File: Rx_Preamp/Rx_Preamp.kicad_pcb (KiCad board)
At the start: 2 copper layers, 97.5 x 79.5 mm, 128 parts, among them J1 Conn_Coaxial, J2 Conn_Coaxial, J3 Conn_Coaxial, J4 Conn_Coaxial, J5 Barrel_Jack_Switch, J6 Barrel_Jack_Switch, J7 ScrewTerminal01x03, SW1 SW_DIP_x04, U1 AD8429, U2 LT6350HMS8TRPBF, U3 ADA4610-1ARJZ, U4 ADA4610-1ARJZ, U5 L7805, U6 L7905, U7 ADA4610-1ARJZ, U8 PIG-LOGO, U9 PIG-LOGO

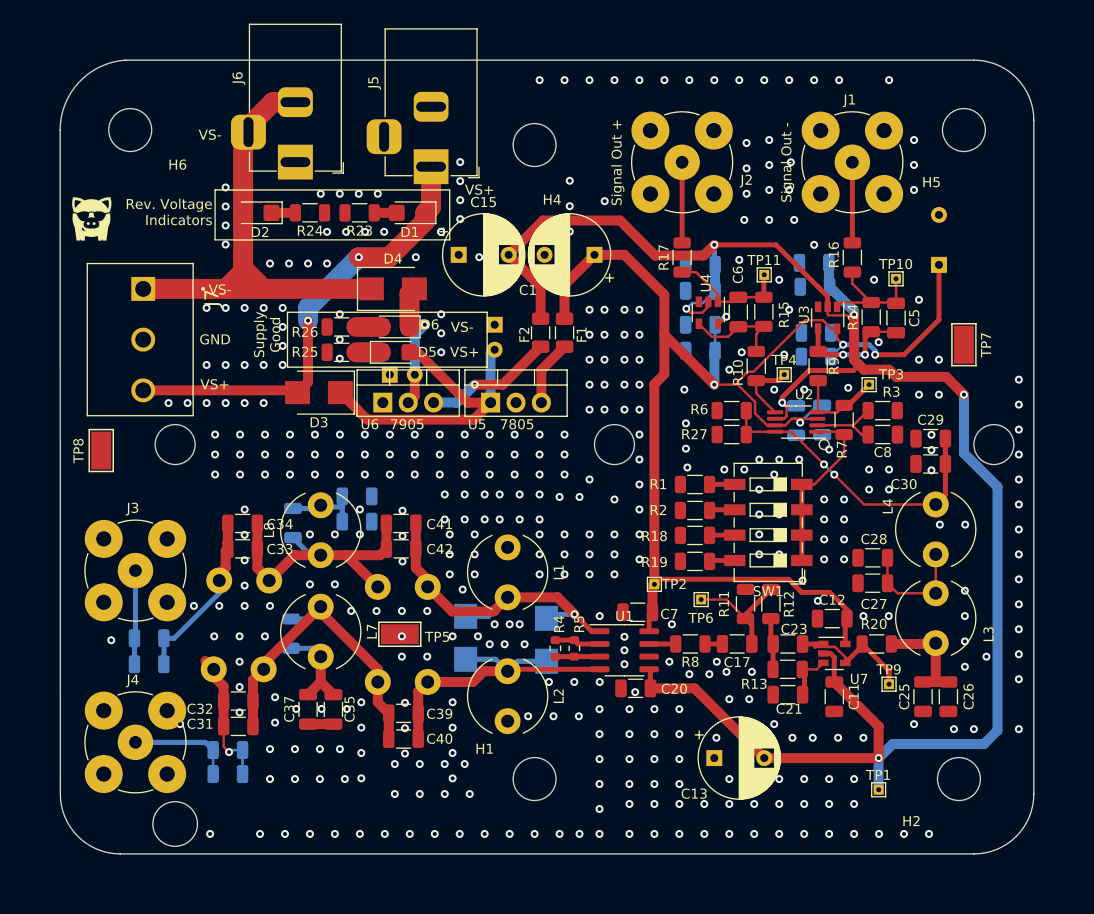
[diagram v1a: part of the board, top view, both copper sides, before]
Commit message: Modular(JFET) preamp and INA preamp
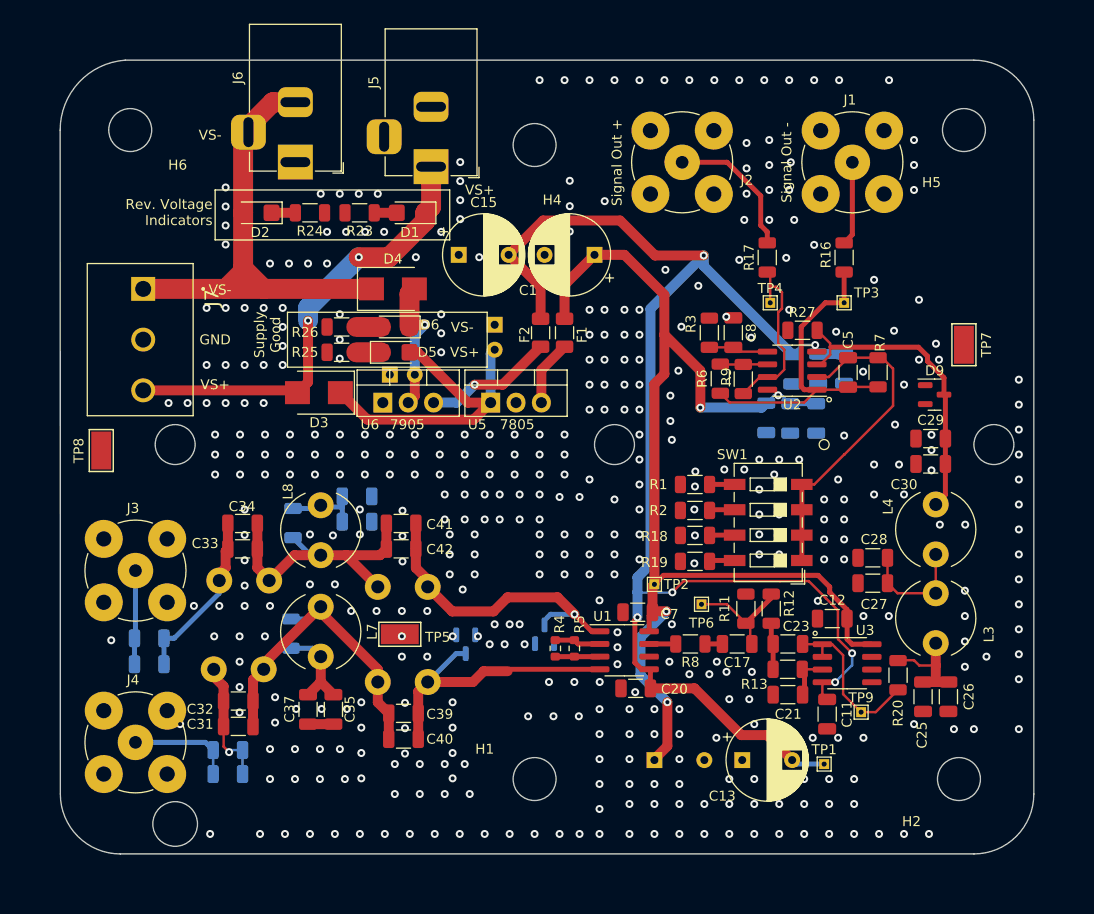
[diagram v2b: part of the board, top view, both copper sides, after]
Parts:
- removed C10, C14: 1u, Capacitor_SMD:C_1206_3216Metric
- removed C19, C4: 100n, Capacitor_SMD:C_1206_3216Metric
- removed C6: 300p, Capacitor_SMD:C_1206_3216Metric
- removed L1, L2: 1m, Inductor_THT:L_Radial_D7.8mm_P5.00mm_Fastron_07HCP
- removed R10, R14, R15: 1k, Resistor_SMD:R_1206_3216Metric
- removed TP10, TP11: TestPoint, TestPoint:TestPoint_THTPad_1.0x1.0mm_Drill0.5mm
- removed U4, U7: ADA4610-1ARJZ, Package_TO_SOT_SMD:SOT-23-5
- removed U8: PIG-LOGO, PigLogos:PIG-LOGO2
- removed U9: PIG-LOGO, Symbol:OSHW-Symbol_22.3x20mm_SilkScreen
- added D9: BAV99, Package_TO_SOT_SMD:SOT-23, F.Cu at (130.1, 116.0)
- C5: value 300p -> 62p
- D7, D8: value D -> BAV99; footprint Diode_SMD:D_SMB -> Package_TO_SOT_SMD:SOT-23
- R16, R17: value 49.9 -> 47
- R6: value 470 -> 1k
- U2: value LT6350HMS8TRPBF -> ADA4075-2; footprint Package_SO:MSOP-8_3x3mm_P0.65mm -> Package_SO:SOIC-8_3.9x4.9mm_P1.27mm
- U3: value ADA4610-1ARJZ -> ADA4075-2; footprint Package_TO_SOT_SMD:SOT-23-5 -> Package_SO:SOIC-8_3.9x4.9mm_P1.27mm
- moved C2 57.2 mm to (102.0, 152.6), turned to 0 degrees
- moved U3 34.7 mm to (121.3, 142.9), turned to 0 degrees
- moved R3 19.0 mm to (107.5, 109.8), turned to 90 degrees
- moved C8 18.1 mm to (109.9, 109.8), turned to 90 degrees
- moved C16 16.4 mm to (121.0, 113.4), turned to 90 degrees
- moved C18 15.7 mm to (118.4, 113.4), turned to 90 degrees
- moved C9 13.4 mm to (118.2, 118.4), turned to 90 degrees
- moved C24 13.0 mm to (115.6, 118.4), turned to 90 degrees
- moved R27 12.6 mm to (116.8, 109.6)
- moved TP3 8.57 mm to (121.0, 106.8)
- moved R17 8.52 mm to (113.3, 102.3)
- moved R9 7.61 mm to (110.9, 114.4), turned to -90 degrees
- moved TP4 7.33 mm to (113.6, 106.8)
- moved C5 7.26 mm to (121.4, 113.8)
- moved TP1 6.04 mm to (119.0, 153.0)
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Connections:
- C5 pad 1: /Out1-AmpOut -> /SE2D-In-
- C5 pad 2: /Out1-AmpV- -> /SE2D-Out1
- D7 pad 1: SigFilt+ -> GND
- D7 pad 2: SigFilt- -> GND
- D8 pad 1: SigFilt- -> GND
- D8 pad 2: SigFilt+ -> GND
- R16 pad 1: /Out1-AmpOut -> /SE2D-Out1
- R17 pad 1: /Out2-AmpOut -> /SE2D-Out2
- R6 pad 1: SE2D_IN+ -> /SE2D-Out1
- R6 pad 2: GND -> Net-(R6-Pad2)
- R9 pad 1: /SE2D-Out1 -> Net-(R6-Pad2)
- R9 pad 2: /Out1-AmpV- -> /SE2D-Out2
- U2 pad 1: /SE2D-In- -> /SE2D-Out1
- U2 pad 2: /SE2D-In2+ -> /SE2D-In-
- U2 pad 3: +5V -> SE2D_IN+
- U2 pad 4: /SE2D-Out1 -> -5V
- U2 pad 5: /SE2D-Out2 -> /SE2D-In2+
- U2 pad 6: -5V -> Net-(R6-Pad2)
- U2 pad 7: +5V -> /SE2D-Out2
- U2 pad 8: SE2D_IN+ -> +5V
- U3 pad 1: /Out1-AmpOut -> /AA-PreFilt
- U3 pad 2: -5V -> /AA-PreFilt
- U3 pad 3: GND -> /AA-IN+
- U3 pad 4: /Out1-AmpV- -> -5V
- U3 pad 5: +5V -> (no net)
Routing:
- net -5V: track 190.3 -> 152.1 mm
- net +5V: track 143.6 -> 119.2 mm, vias 5 -> 4
- net /SE2D-Out1: track 9.53 -> 32.9 mm
- net /SE2D-In-: track 17.9 -> 32.6 mm
- net /Out1-AmpOut: track 12.4 -> 0.00 mm
- net /Out2-AmpOut: track 12.3 -> 0.00 mm
- net /Out1-AmpV-: track 12.2 -> 0.00 mm, vias 2 -> 0
- net /SE2D-Out2: track 7.00 -> 17.8 mm
- net /Out2-AmpV-: track 10.3 -> 0.00 mm
- net /Out-: track 8.09 -> 14.2 mm
- net SigFilt+: track 35.0 -> 30.0 mm
- net Net-(R6-Pad2): track 0.00 -> 4.74 mm
- net SigFilt-: track 32.9 -> 28.8 mm
- net /SE2D-In2+: track 7.66 -> 6.00 mm
- net SigIn-: track 13.9 -> 12.8 mm
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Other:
- net class Default removed
- board text added: "MPI Rx Filter+Preamp 20FEB2023 Rev. B"
- board text removed: "MPI Rx Filter+Preamp 30MAY2021 Rev. B"
